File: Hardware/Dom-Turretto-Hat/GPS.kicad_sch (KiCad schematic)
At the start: 6 parts

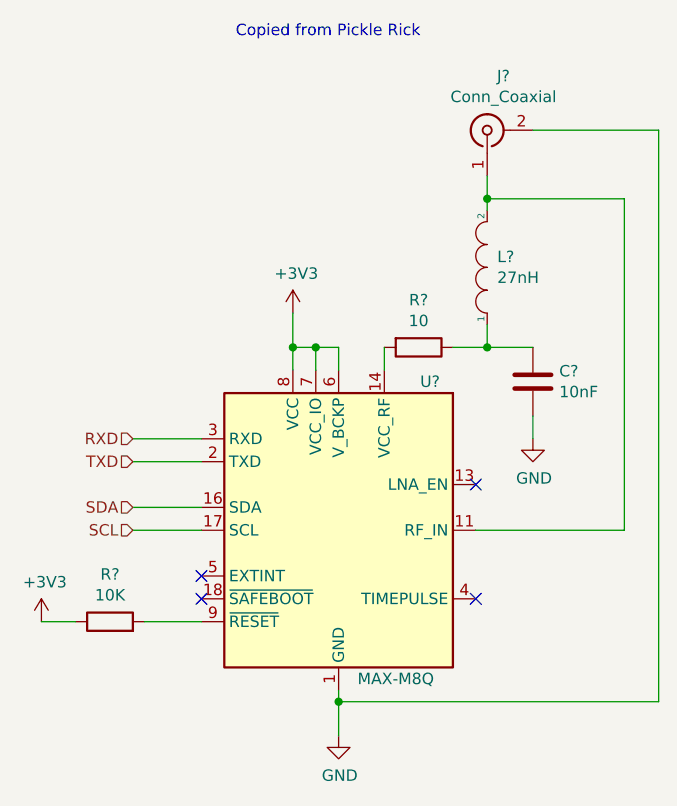
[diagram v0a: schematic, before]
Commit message: Assigned footprints
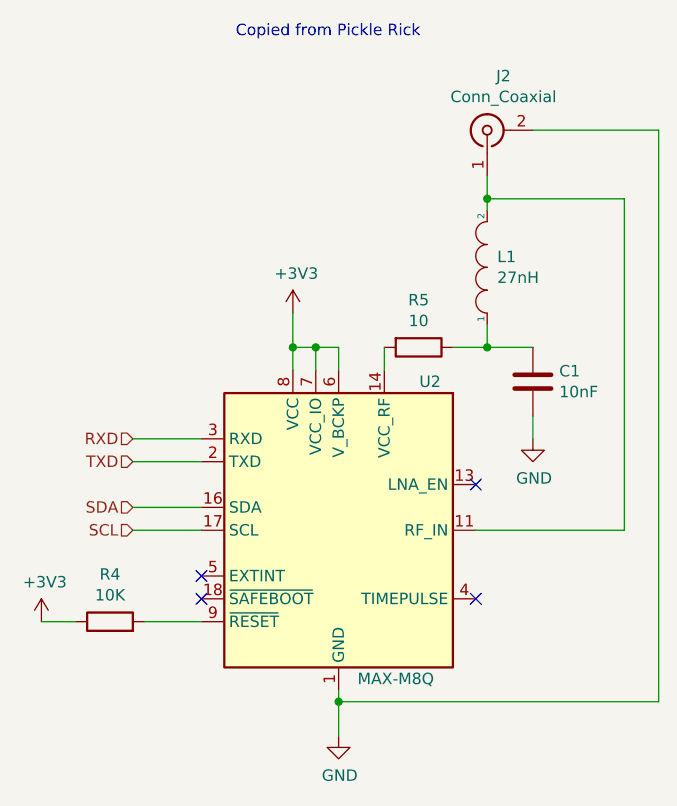
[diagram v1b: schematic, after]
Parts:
- gave numbers to parts that had none: 6
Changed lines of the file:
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@@
   (symbol (lib_id "power:GND") (at 147.32 121.92 0) (unit 1)
     (in_bom yes) (on_board yes)
-    (property "Reference" "#PWR?" (id 0) (at 147.32 128.27 0)
+    (property "Reference" "#PWR011" (id 0) (at 147.32 128.27 0)
       (effects (font (size 1.27 1.27)) hide)
     )
@@
   (symbol (lib_id "Device:C") (at 168.91 82.55 0) (unit 1)
     (in_bom yes) (on_board yes)
-    (property "Reference" "C?" (id 0) (at 171.831 81.3816 0)
+    (property "Reference" "C1" (id 0) (at 171.831 81.3816 0)
       (effects (font (size 1.27 1.27)) (justify left))
     )
@@
   (symbol (lib_id "RF_GPS:MAX-M8Q") (at 147.32 99.06 0) (unit 1)
     (in_bom yes) (on_board yes)
-    (property "Reference" "U?" (id 0) (at 157.48 82.55 0))
+    (property "Reference" "U2" (id 0) (at 157.48 82.55 0))
     (property "Value" "MAX-M8Q" (id 1) (at 153.67 115.57 0))
     (property "Footprint" "RF_GPS:ublox_MAX" (id 2) (at 157.48 115.57 0)
@@
   (symbol (lib_id "Connector:Conn_Coaxial") (at 163.83 54.61 90) (unit 1)
     (in_bom yes) (on_board yes)
-    (property "Reference" "J?" (id 0) (at 165.6334 48.5902 90))
+    (property "Reference" "J2" (id 0) (at 165.6334 48.5902 90))
     (property "Value" "Conn_Coaxial" (id 1) (at 165.6334 50.9016 90))
     (property "Footprint" "Connector_Coaxial:SMA_Molex_73251-1153_EdgeMount_Horizontal" (id 2) (at 163.83 54.61 0)
@@
   (symbol (lib_id "power:+3V3") (at 142.24 74.93 0) (unit 1)
     (in_bom yes) (on_board yes)
-    (property "Reference" "#PWR?" (id 0) (at 142.24 78.74 0)
+    (property "Reference" "#PWR010" (id 0) (at 142.24 78.74 0)
       (effects (font (size 1.27 1.27)) hide)
     )
@@
   (symbol (lib_id "Device:R") (at 156.21 78.74 270) (unit 1)
     (in_bom yes) (on_board yes)
-    (property "Reference" "R?" (id 0) (at 156.21 73.4822 90))
+    (property "Reference" "R5" (id 0) (at 156.21 73.4822 90))
     (property "Value" "10" (id 1) (at 156.21 75.7936 90))
     (property "Footprint" "Resistor_SMD:R_0603_1608Metric" (id 2) (at 156.21 76.962 90)
@@
   (symbol (lib_id "Device:R") (at 121.92 109.22 90) (unit 1)
     (in_bom yes) (on_board yes)
-    (property "Reference" "R?" (id 0) (at 121.92 103.9622 90))
+    (property "Reference" "R4" (id 0) (at 121.92 103.9622 90))
     (property "Value" "10K" (id 1) (at 121.92 106.2736 90))
     (property "Footprint" "Resistor_SMD:R_0603_1608Metric" (id 2) (at 121.92 110.998 90)
@@
   (symbol (lib_id "power:GND") (at 168.91 88.9 0) (unit 1)
     (in_bom yes) (on_board yes)
-    (property "Reference" "#PWR?" (id 0) (at 168.91 95.25 0)
+    (property "Reference" "#PWR012" (id 0) (at 168.91 95.25 0)
       (effects (font (size 1.27 1.27)) hide)
     )
@@
   (symbol (lib_id "pspice:INDUCTOR") (at 163.83 69.85 90) (unit 1)
     (in_bom yes) (on_board yes)
-    (property "Reference" "L?" (id 0) (at 164.9476 68.6816 90)
+    (property "Reference" "L1" (id 0) (at 164.9476 68.6816 90)
       (effects (font (size 1.27 1.27)) (justify right))
     )
@@
   (symbol (lib_id "power:+3V3") (at 114.3 109.22 0) (unit 1)
     (in_bom yes) (on_board yes)
-    (property "Reference" "#PWR?" (id 0) (at 114.3 113.03 0)
+    (property "Reference" "#PWR09" (id 0) (at 114.3 113.03 0)
       (effects (font (size 1.27 1.27)) hide)
     )
